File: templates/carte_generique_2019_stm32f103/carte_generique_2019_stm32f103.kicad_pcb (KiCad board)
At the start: 2 copper layers, 27 parts, among them J1 Connecteur_blackpill_gauche, J2 Alim puissance, J3 Alim logique, J4 Connecteur_blackpill_droite, J5 PWM input, J6 PWM output, J7 QEI, J8 Liaison serie, Q1 PMF370XN, Q2 2N7000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

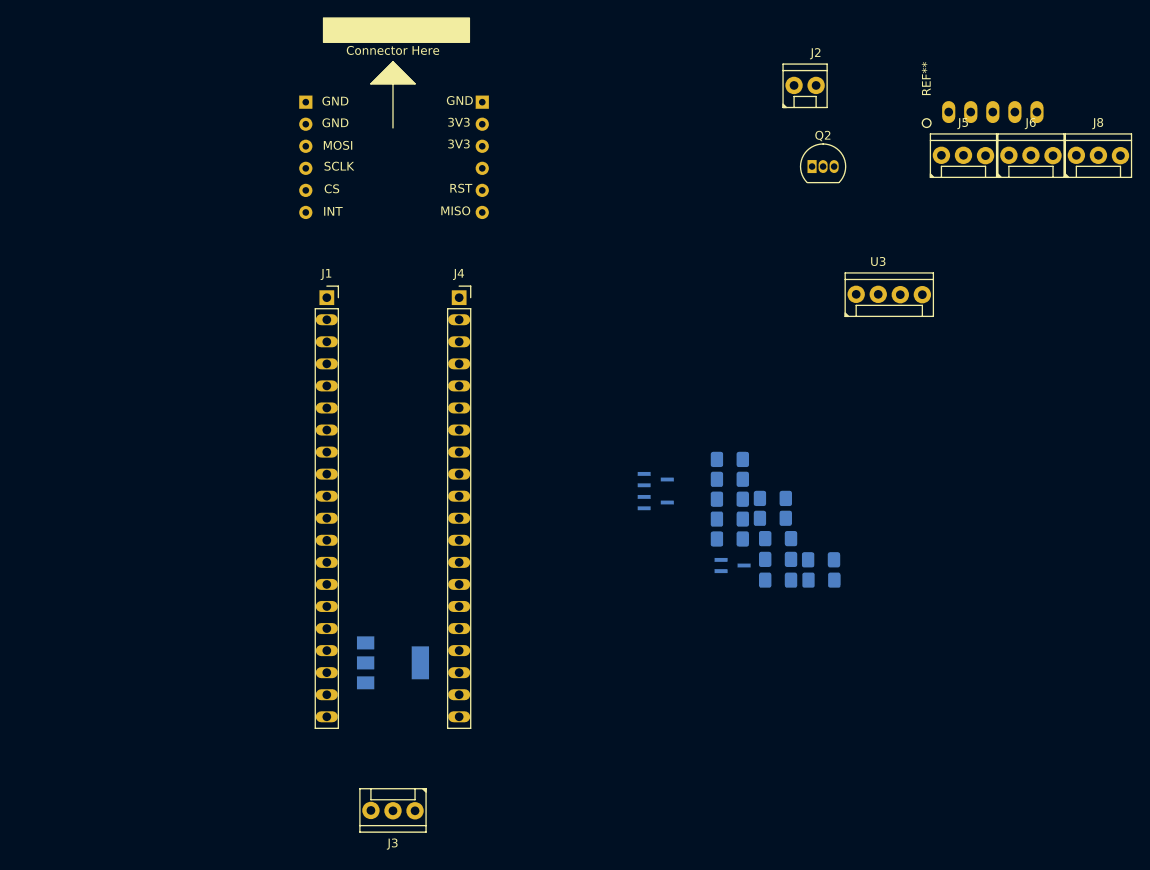
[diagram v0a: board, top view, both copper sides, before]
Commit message: move around some footprints
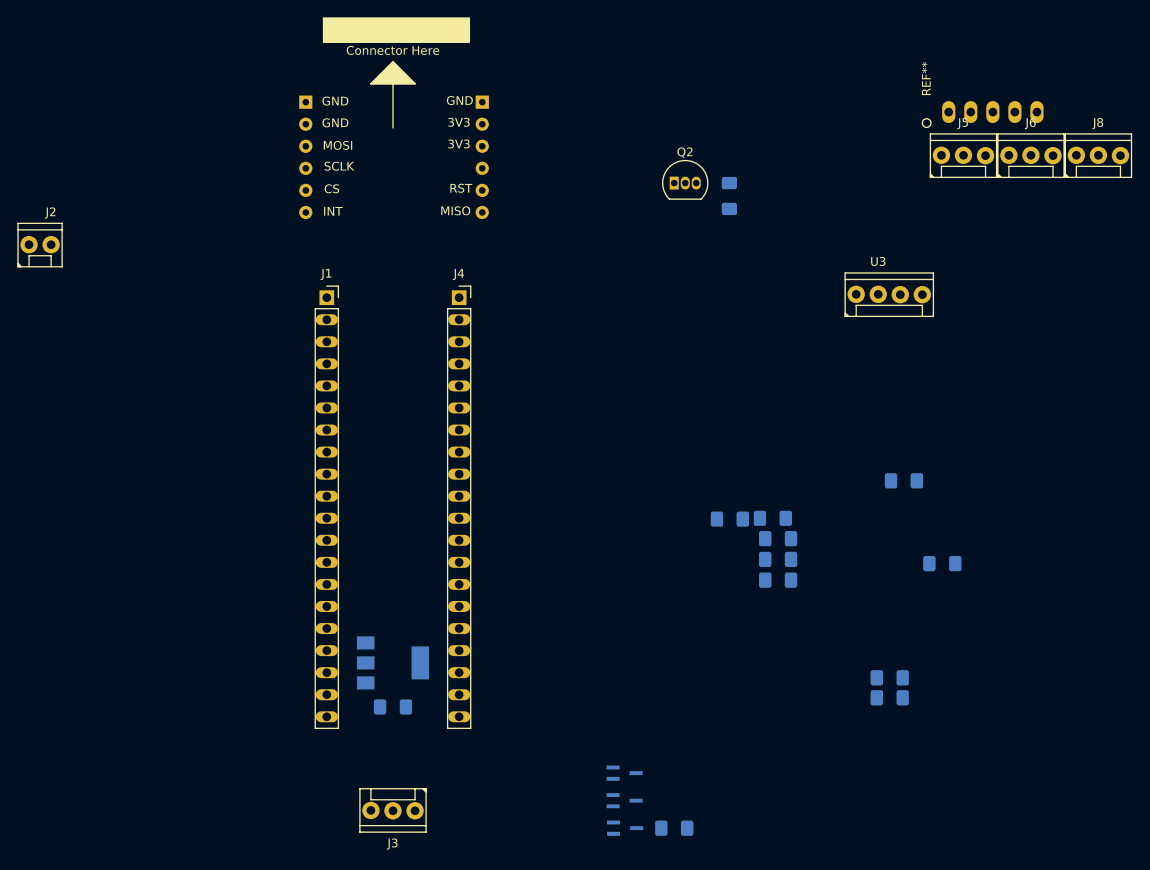
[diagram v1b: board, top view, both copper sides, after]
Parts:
- moved J2 90.0 mm to (85.1, 69.2)
- moved C1 43.3 mm to (124.5, 123.2)
- moved Q3 37.7 mm to (151.2, 137.1)
- moved Q4 37.2 mm to (151.1, 134.0)
- moved R3 35.2 mm to (163.2, 64.4), turned to 90 degrees
- moved D2 33.2 mm to (156.8, 137.2)
- moved R1 29.4 mm to (181.7, 122.1)
- moved R4 29.4 mm to (181.7, 119.8)
- moved Q1 26.9 mm to (151.1, 130.8)
- moved R5 20.2 mm to (183.3, 97.2)
- moved Q2 16.0 mm to (156.8, 62.9)
- moved R6 14.0 mm to (187.7, 106.7)
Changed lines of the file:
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@@
   )
   (module @Robot:HE14-2-straight (layer F.Cu)
-    (at 173.185001 50.875001)
+    (at 85.09 69.215)
     (tags "HE14 3 straight connector 1x3")
     (fp_text reference J2 (at 0 -3) (layer F.SilkS)
@@
   )
   (module Capacitor_SMD:C_1206_3216Metric_Pad1.42x1.75mm_HandSolder (layer B.Cu)
-    (at 163.25289 103.84741)
+    (at 124.46 123.19)
     (descr "Capacitor SMD 1206 (3216 Metric), square (rectangular) end terminal, IPC_7351 nominal with elongated pad for handsoldering. (Body size source: http://www.tortai-tech.com/upload/download/2011102023233369053.pdf), generated with kicad-footprint-generator")
     (tags "capacitor handsolder")
@@
   )
   (module LED_SMD:LED_1206_3216Metric_Pad1.42x1.75mm_HandSolder (layer B.Cu)
-    (at 173.79789 108.58741)
+    (at 156.845 137.16)
     (descr "LED SMD 1206 (3216 Metric), square (rectangular) end terminal, IPC_7351 nominal, (Body size source: http://www.tortai-tech.com/upload/download/2011102023233369053.pdf), generated with kicad-footprint-generator")
     (tags "LED handsolder")
@@
   )
   (module Package_TO_SOT_SMD:SOT-323_SC-70_Handsoldering (layer B.Cu)
-    (at 163.565001 106.903855)
+    (at 151.13 130.81)
     (descr "SOT-323, SC-70 Handsoldering")
     (tags "SOT-323 SC-70 Handsoldering")
@@
   )
   (module Package_TO_SOT_THT:TO-92_Inline (layer F.Cu)
-    (at 172.72 60.96)
+    (at 156.845 62.865)
     (descr "TO-92 leads in-line, narrow, oval pads, drill 0.75mm (see NXP sot054_po.pdf)")
     (tags "to-92 sc-43 sc-43a sot54 PA33 transistor")
@@
   )
   (module Package_TO_SOT_SMD:SOT-323_SC-70_Handsoldering (layer B.Cu)
-    (at 154.715001 99.653855)
+    (at 151.19 137.145)
     (descr "SOT-323, SC-70 Handsoldering")
     (tags "SOT-323 SC-70 Handsoldering")
@@
   )
   (module Package_TO_SOT_SMD:SOT-323_SC-70_Handsoldering (layer B.Cu)
-    (at 154.715001 97.003855)
+    (at 151.13 133.985)
     (descr "SOT-323, SC-70 Handsoldering")
     (tags "SOT-323 SC-70 Handsoldering")
@@
   )
   (module Resistor_SMD:R_1206_3216Metric_Pad1.42x1.75mm_HandSolder (layer B.Cu)
-    (at 163.25289 99.26741)
+    (at 181.66789 122.12741)
     (descr "Resistor SMD 1206 (3216 Metric), square (rectangular) end terminal, IPC_7351 nominal with elongated pad for handsoldering. (Body size source: http://www.tortai-tech.com/upload/download/2011102023233369053.pdf), generated with kicad-footprint-generator")
     (tags "resistor handsolder")
@@
   )
   (module Resistor_SMD:R_1206_3216Metric_Pad1.42x1.75mm_HandSolder (layer B.Cu)
-    (at 168.20289 99.17741)
+    (at 163.195 64.3525 90)
     (descr "Resistor SMD 1206 (3216 Metric), square (rectangular) end terminal, IPC_7351 nominal with elongated pad for handsoldering. (Body size source: http://www.tortai-tech.com/upload/download/2011102023233369053.pdf), generated with kicad-footprint-generator")
     (tags "resistor handsolder")
     (attr smd)
-    (fp_text reference R3 (at 0 1.82) (layer B.SilkS)
-      (effects (font (size 1 1) (thickness 0.15)) (justify mirror))
-    )
-    (fp_text value 10k (at 0 -1.82) (layer B.Fab)
+    (fp_text reference R3 (at 0 1.82 90) (layer B.SilkS)
+      (effects (font (size 1 1) (thickness 0.15)) (justify mirror))
+    )
+    (fp_text value 10k (at 0 -1.82 90) (layer B.Fab)
       (effects (font (size 1 1) (thickness 0.15)) (justify mirror))
     )
@@
     (fp_line (start 2.45 1.12) (end 2.45 -1.12) (layer B.CrtYd) (width 0.05))
     (fp_line (start 2.45 -1.12) (end -2.45 -1.12) (layer B.CrtYd) (width 0.05))
-    (fp_text user %R (at 0 0) (layer B.Fab)
-      (effects (font (size 0.8 0.8) (thickness 0.12)) (justify mirror))
-    )
-    (pad 1 smd roundrect (at -1.4875 0) (size 1.425 1.75) (layers B.Cu B.Paste B.Mask) (roundrect_rratio 0.175439)
+    (fp_text user %R (at 0 0 90) (layer B.Fab)
+      (effects (font (size 0.8 0.8) (thickness 0.12)) (justify mirror))
+    )
+    (pad 1 smd roundrect (at -1.4875 0 90) (size 1.425 1.75) (layers B.Cu B.Paste B.Mask) (roundrect_rratio 0.175439)
       (net 1 +5V))
-    (pad 2 smd roundrect (at 1.4875 0) (size 1.425 1.75) (layers B.Cu B.Paste B.Mask) (roundrect_rratio 0.175439)
+    (pad 2 smd roundrect (at 1.4875 0 90) (size 1.425 1.75) (layers B.Cu B.Paste B.Mask) (roundrect_rratio 0.175439)
       (net 57 /5V_logic))
     (model ${KISYS3DMOD}/Resistor_SMD.3dshapes/R_1206_3216Metric.wrl
@@
   )
   (module Resistor_SMD:R_1206_3216Metric_Pad1.42x1.75mm_HandSolder (layer B.Cu)
-    (at 163.25289 96.97741)
+    (at 181.66789 119.83741)
     (descr "Resistor SMD 1206 (3216 Metric), square (rectangular) end terminal, IPC_7351 nominal with elongated pad for handsoldering. (Body size source: http://www.tortai-tech.com/upload/download/2011102023233369053.pdf), generated with kicad-footprint-generator")
     (tags "resistor handsolder")
@@
   )
   (module Resistor_SMD:R_1206_3216Metric_Pad1.42x1.75mm_HandSolder (layer B.Cu)
-    (at 163.25289 94.68741)
+    (at 183.2975 97.155)
     (descr "Resistor SMD 1206 (3216 Metric), square (rectangular) end terminal, IPC_7351 nominal with elongated pad for handsoldering. (Body size source: http://www.tortai-tech.com/upload/download/2011102023233369053.pdf), generated with kicad-footprint-generator")
     (tags "resistor handsolder")
@@
   )
   (module Resistor_SMD:R_1206_3216Metric_Pad1.42x1.75mm_HandSolder (layer B.Cu)
-    (at 173.75289 106.24741)
+    (at 187.72289 106.68)
     (descr "Resistor SMD 1206 (3216 Metric), square (rectangular) end terminal, IPC_7351 nominal with elongated pad for handsoldering. (Body size source: http://www.tortai-tech.com/upload/download/2011102023233369053.pdf), generated with kicad-footprint-generator")
     (tags "resistor handsolder")
